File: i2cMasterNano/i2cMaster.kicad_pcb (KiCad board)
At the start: 2 copper layers, 77.5 x 99.1 mm, 27 parts, among them J1 Conn_01x04_Male, J10 Conn_01x01, J2 Conn_01x04_Male, J3 Conn_01x04_Male, J4 Conn_01x04_Male, J5 Conn_01x04_Male, J6 Conn_01x04_Male, J7 Conn_01x04_Male, J8 Conn_01x04_Male, J9 Conn_01x01, SW1 SW_DIP_x03, U1 LM7805_TO220, U2 Arduino_Nano_R3

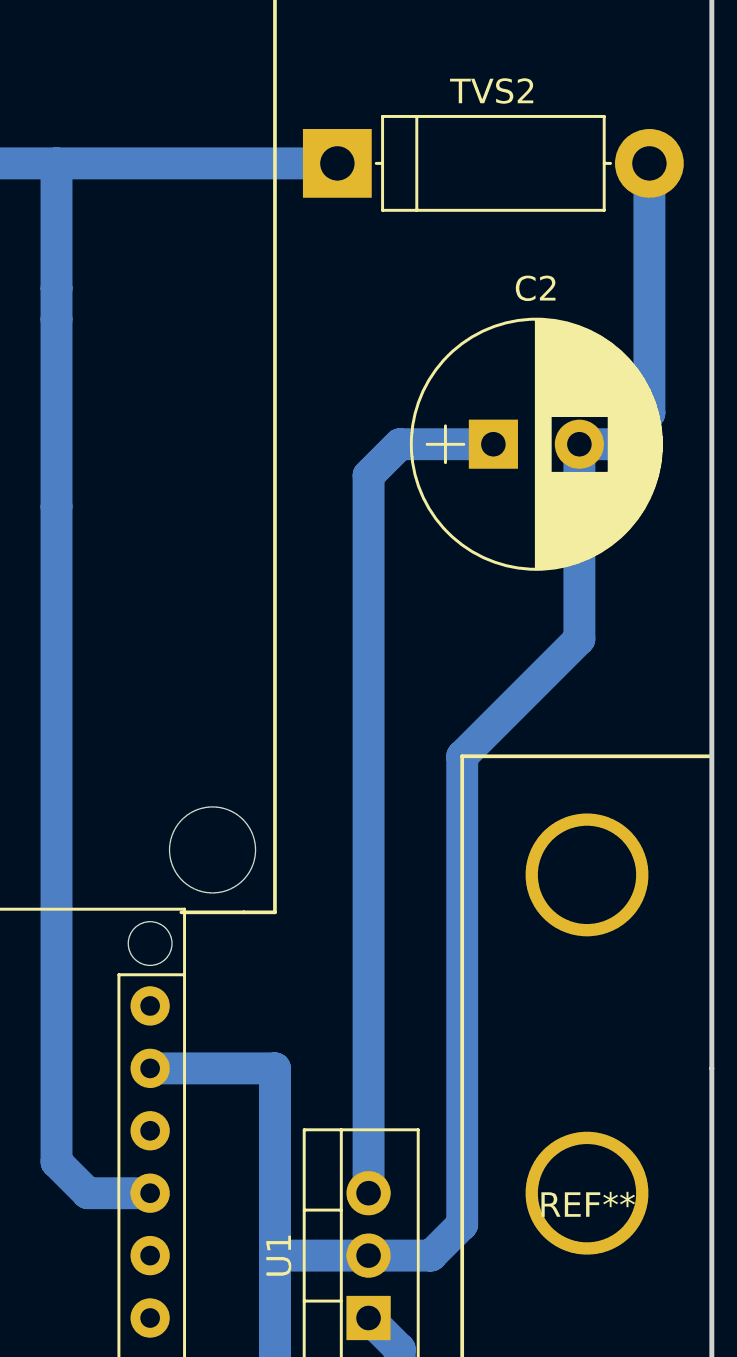
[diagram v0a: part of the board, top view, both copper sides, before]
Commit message: little fix of 5v net
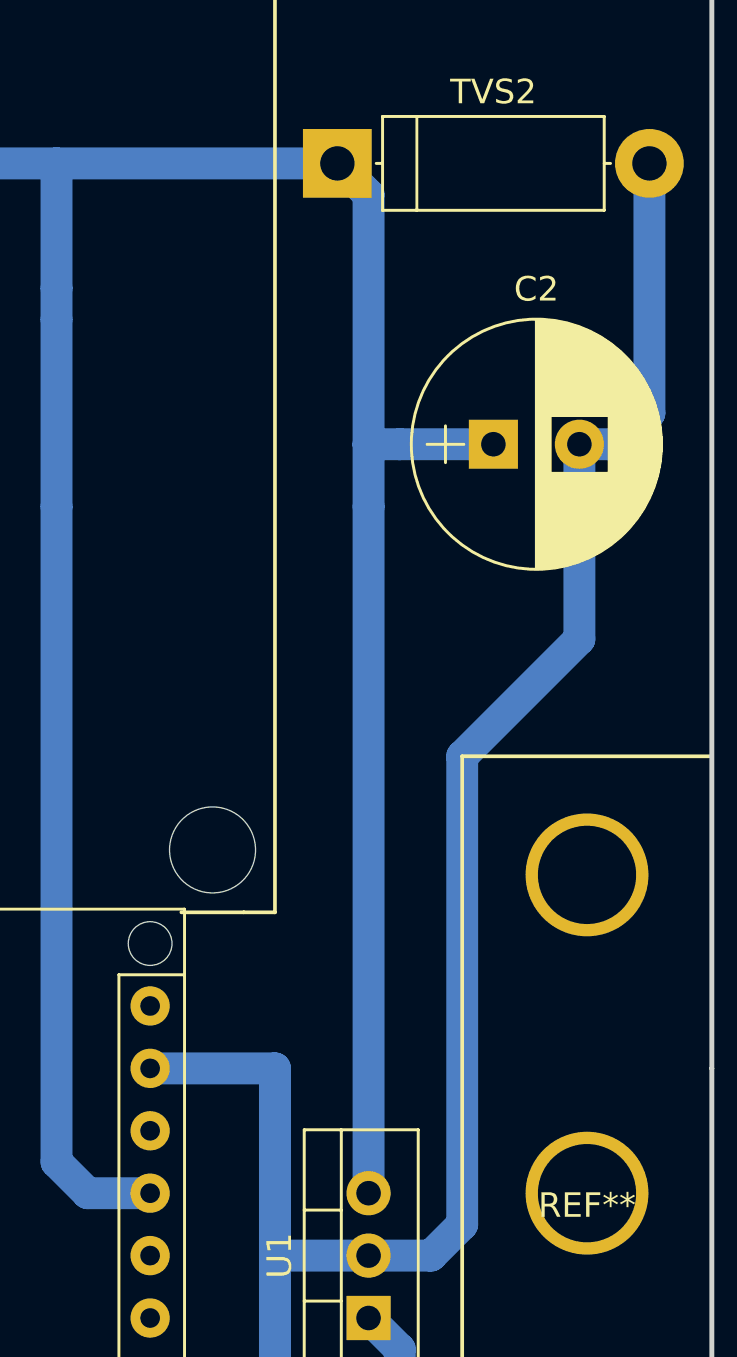
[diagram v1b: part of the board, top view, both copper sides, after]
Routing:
- net +5V: track 241.7 -> 254.4 mm
